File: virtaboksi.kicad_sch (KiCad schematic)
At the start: 21 parts, among them J1 Conn_01x03_Female, J2 Conn_01x02_Female, J3 Conn_01x02_Female, J4 Conn_01x02_Female, J5 Conn_01x02_Female, J6 Conn_01x02_Female, Q1 IRF4905, Q2 IRF4905, Q3 IRF4905

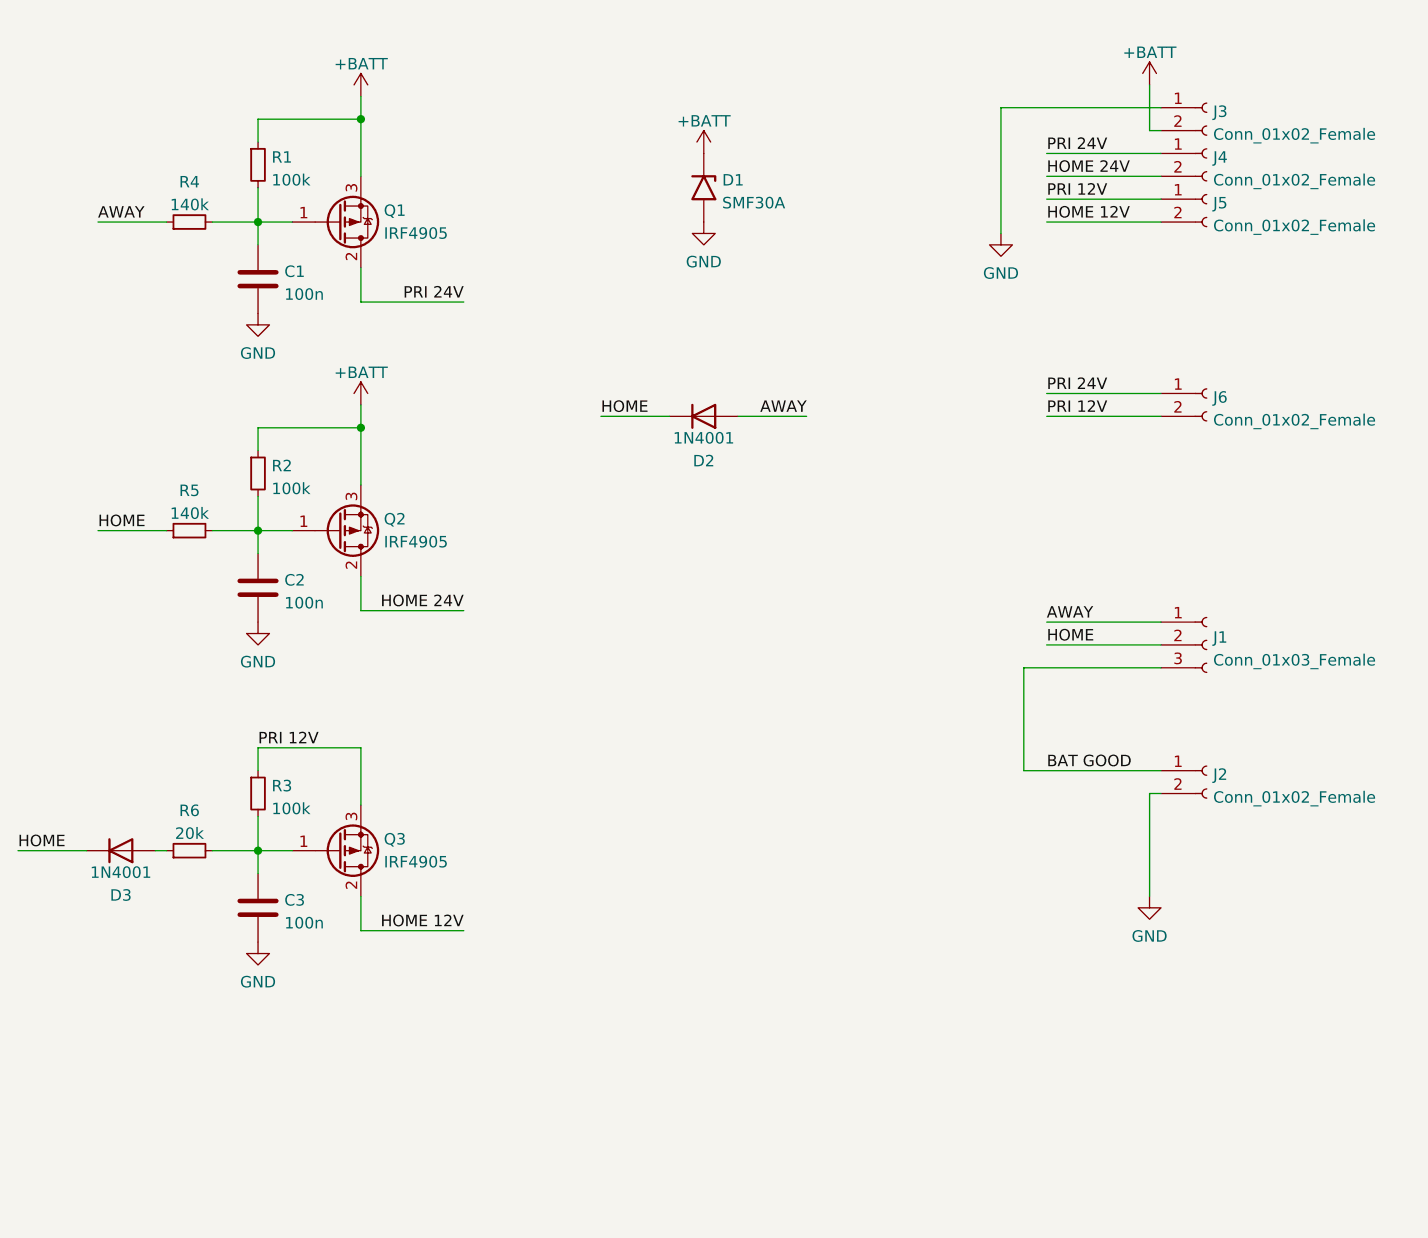
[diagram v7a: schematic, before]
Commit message: Make schematics more readable, no functional changes
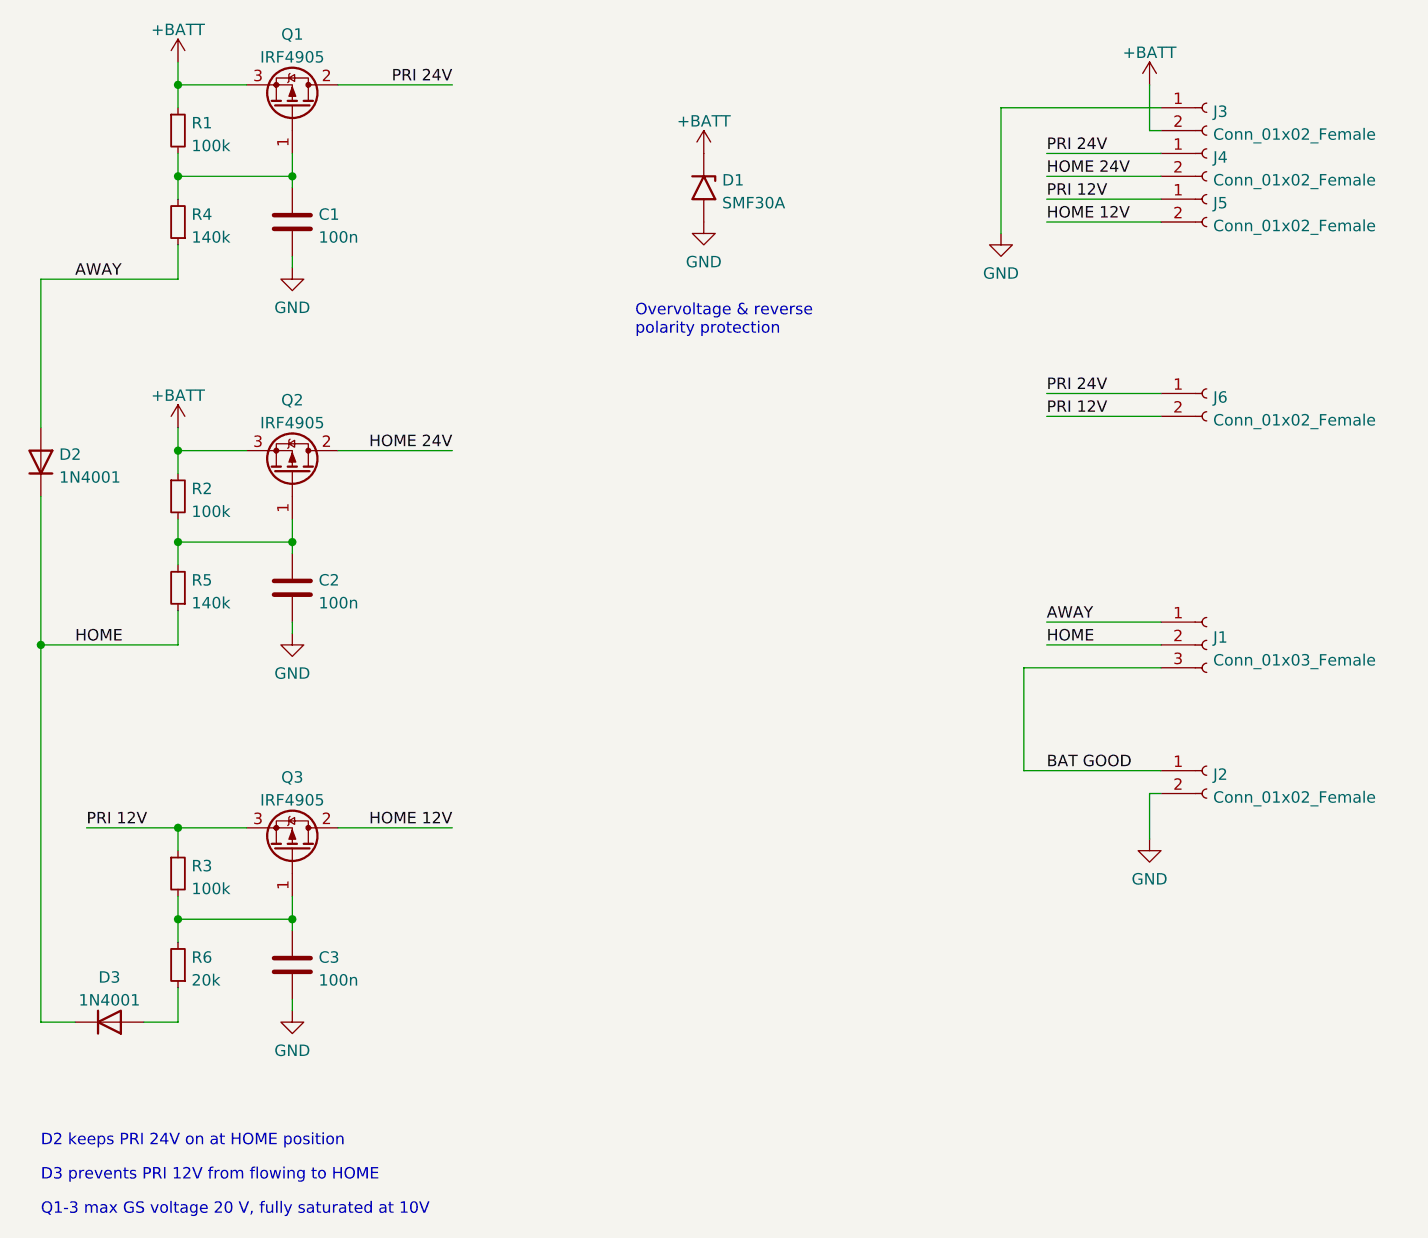
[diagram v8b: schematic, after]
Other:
- note added: "D2 keeps PRI 24V on at HOME position"
- note added: "D3 prevents PRI 12V from flowing to HOME"
- note added: "Overvoltage & reverse polarity protection"
- note added: "Q1-3 max GS voltage 20 V, fully saturated at 10V"
- moved on the sheet: C1, D2, D3, Q1, R1, R4, R6
